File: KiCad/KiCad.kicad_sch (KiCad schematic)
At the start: 24 parts

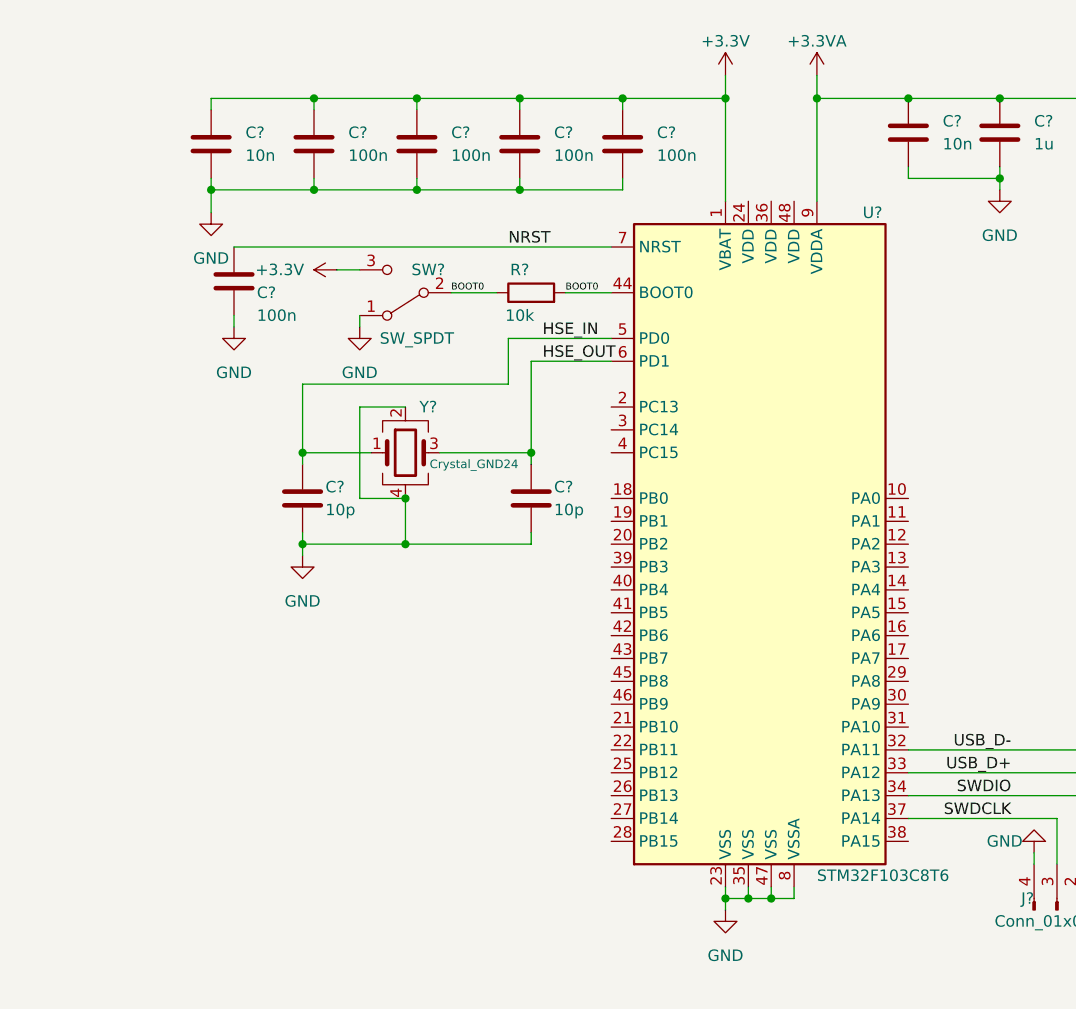
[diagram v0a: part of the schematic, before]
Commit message: Added UART & SPI Support pinout
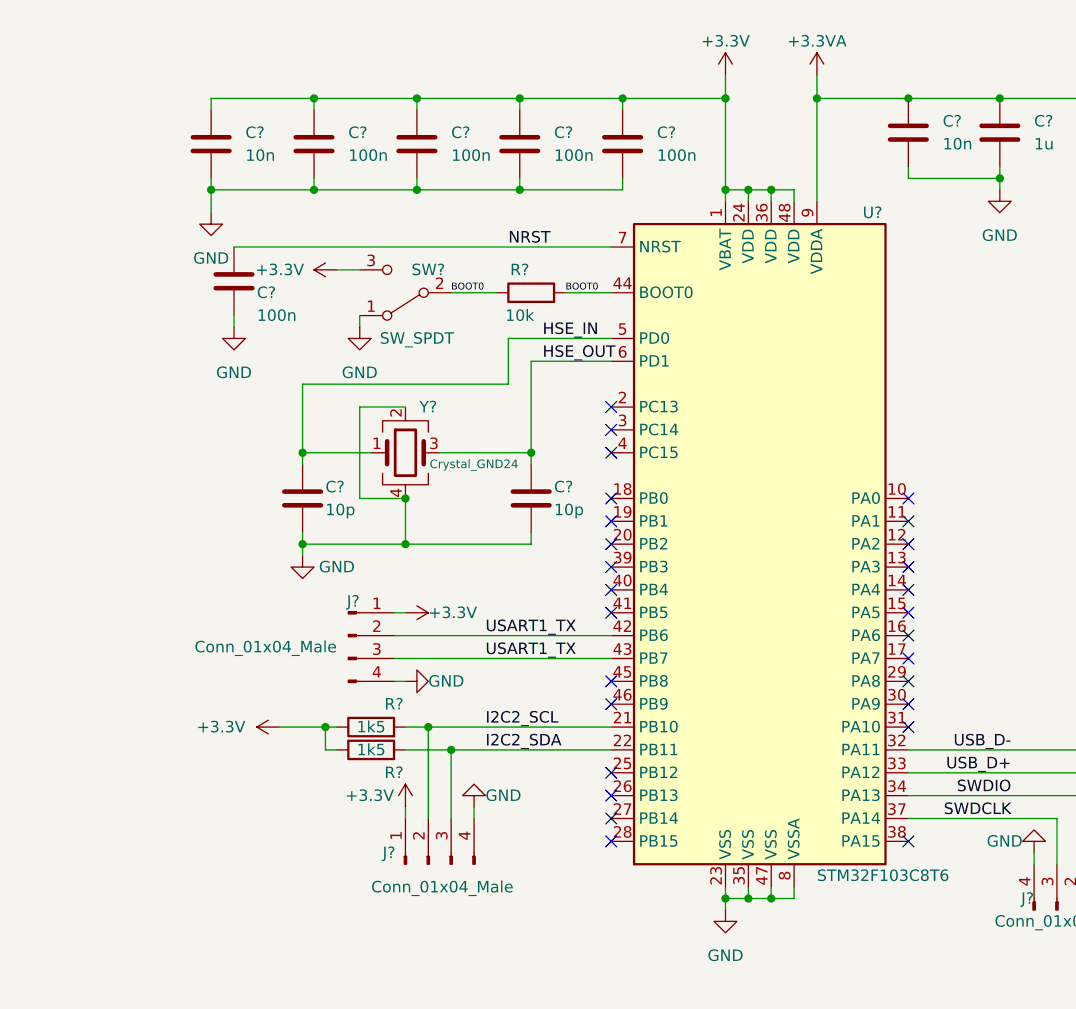
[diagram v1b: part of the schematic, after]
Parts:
- added J? (x2): Conn_01x04_Male, symbol Connector:Conn_01x04_Male
- added R? (x2): 1k5, symbol Device:R
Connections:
- net +3.3V: now also U?.24 (VDD), U?.36 (VDD), U?.48 (VDD), J?.1 (Pin_1), J?.1 (Pin_1), R?.1, R?.1
- net GND: now also J?.4 (Pin_4), J?.4 (Pin_4)
- net I2C2_SCL: now reaches U?.21 (PB10)
- net I2C2_SCL: now also J?.2 (Pin_2), R?.2
- net I2C2_SDA: now reaches U?.22 (PB11)
- net I2C2_SDA: now also J?.3 (Pin_3), R?.2
- net USART1_TX: now reaches U?.42 (PB6)
- net USART1_TX: now also U?.43 (PB7), J?.2 (Pin_2), J?.3 (Pin_3)
- no-connect marks 2 -> 29

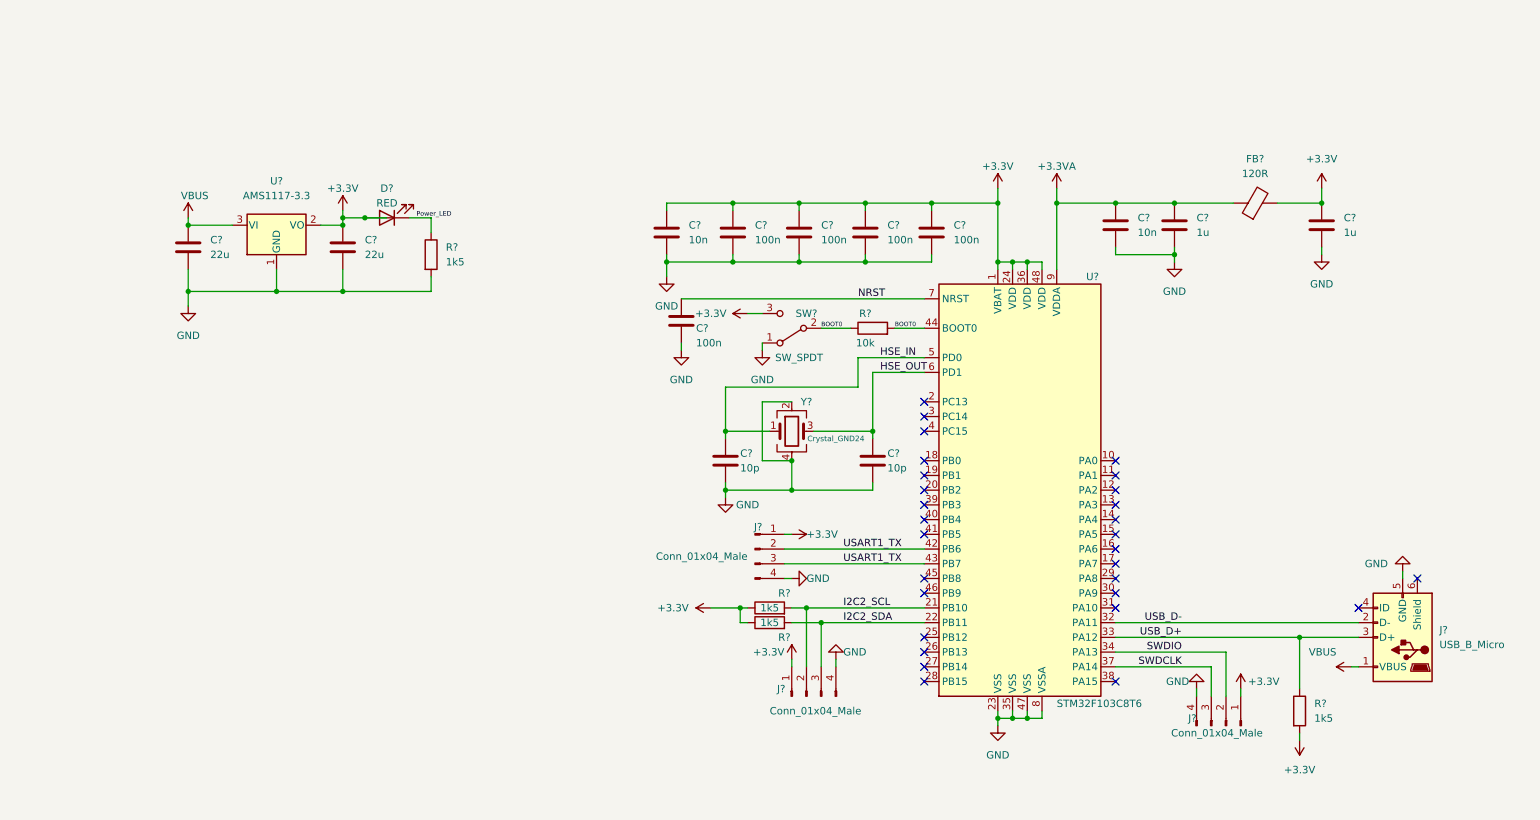
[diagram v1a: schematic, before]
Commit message: Added annotation to schematic
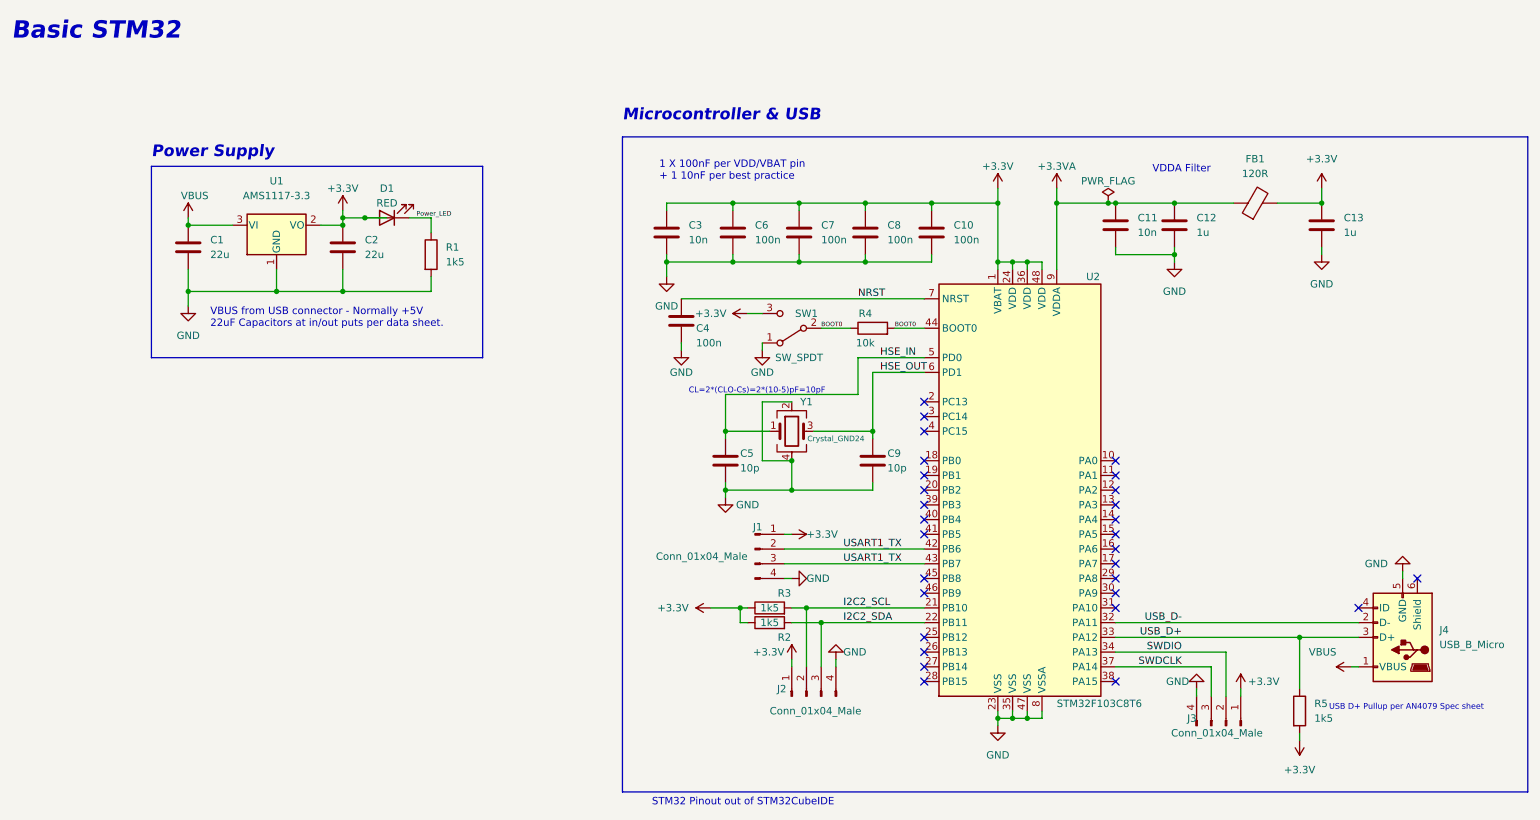
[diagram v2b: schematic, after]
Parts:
- gave numbers to parts that had none: 28
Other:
- note added: "1 X 100nF per VDD/VBAT pin + 1 10nF per best practice"
- note added: "Basic STM32"
- note added: "CL=2*(CLO-Cs)=2*(10-5)pF=10pF"
- note added: "Microcontroller & USB"
- note added: "Power Supply"
- note added: "STM32 Pinout out of STM32CubeIDE"
- note added: "USB D+ Pullup per AN4079 Spec sheet"
- note added: "VBUS from USB connector - Normally +5V 22uF Capacitors at in/out puts per data sheet."
- note added: "VDDA Filter"
- company: (none) -> Sebastian Rincon
- title: (none) -> Basic STM32 Board

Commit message: Added Footprints
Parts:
- C1, C2: footprint (none) -> Capacitor_SMD:C_0805_2012Metric
- C10, C11, C12, C13, C4, C5, C6, C7, C8, C9: footprint (none) -> Capacitor_SMD:C_0402_1005Metric
- C3: value 10n -> 10u; footprint (none) -> Capacitor_SMD:C_0603_1608Metric
- D1: footprint (none) -> LED_SMD:LED_0603_1608Metric
- FB1: footprint (none) -> Inductor_SMD:L_0603_1608Metric
- J1, J2, J3: footprint (none) -> Connector_PinHeader_2.00mm:PinHeader_1x04_P2.00mm_Vertical
- J4: footprint (none) -> Connector_USB:USB_Micro-B_Wuerth_629105150521
- R1, R2, R3, R4, R5: footprint (none) -> Resistor_SMD:R_0402_1005Metric
- SW1: footprint (none) -> Button_Switch_THT:SW_E-Switch_EG1224_SPDT_Angled
- Y1: footprint (none) -> Crystal:Crystal_SMD_3225-4Pin_3.2x2.5mm_HandSoldering
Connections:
- net +3.3V: no longer SW1.3 (C)
- net BOOT0: no longer SW1.2 (B)
- net GND: no longer SW1.1 (A)
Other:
- note added: "1 X 100nF per VDD/VBAT pin + 1 10uF per best practice"
- note removed: "1 X 100nF per VDD/VBAT pin + 1 10nF per best practice"
- moved on the sheet: SW1

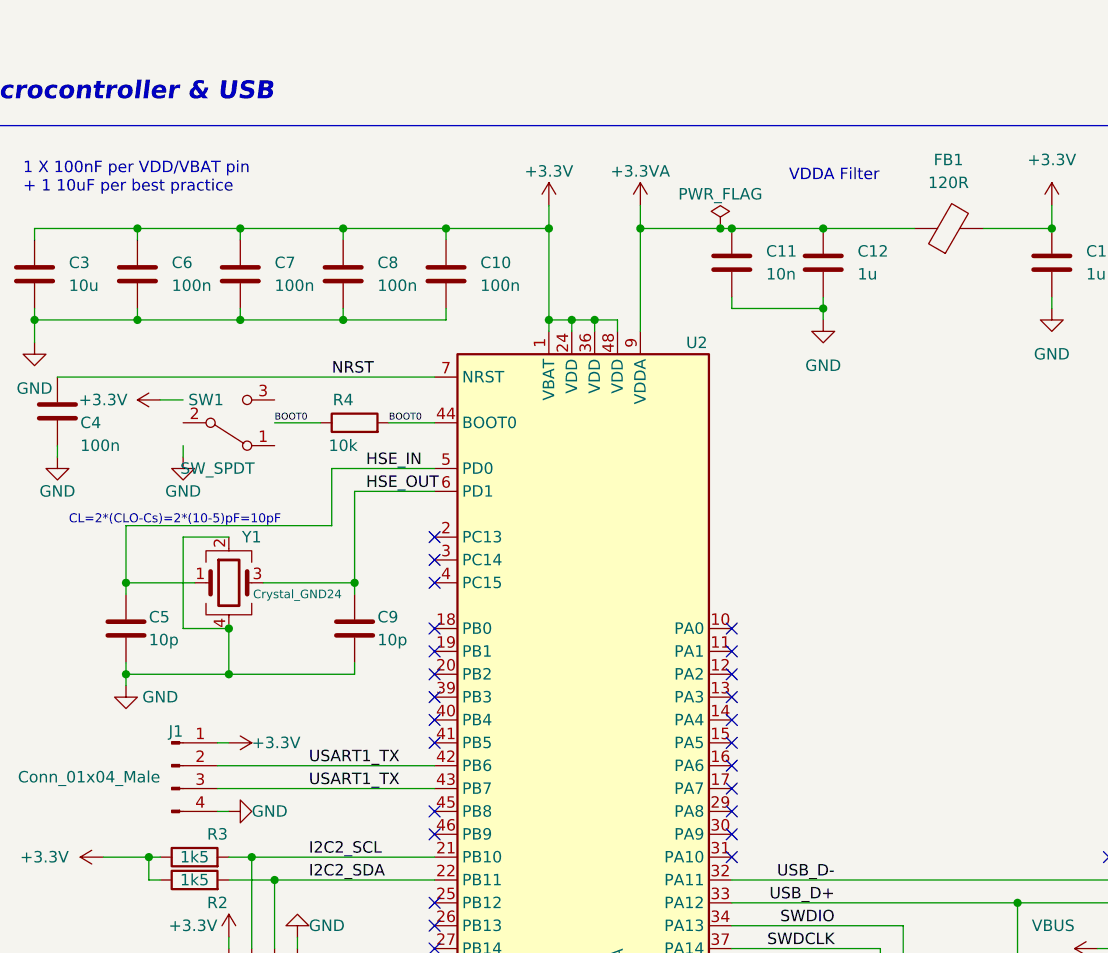
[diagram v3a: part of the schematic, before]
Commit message: Fixed route line bugs & routed pheriphials
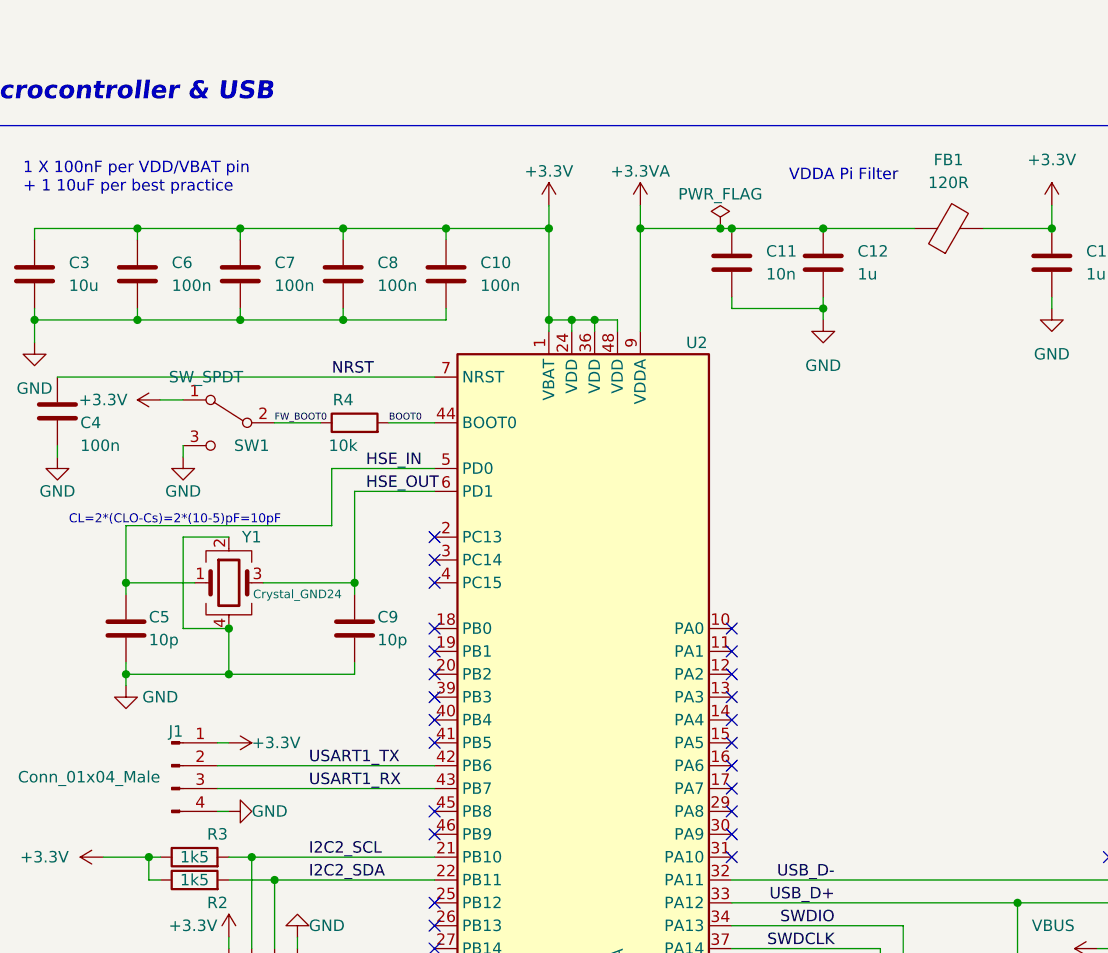
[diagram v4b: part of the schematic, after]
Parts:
- SW1: footprint Button_Switch_THT:SW_E-Switch_EG1224_SPDT_Angled -> Button_Switch_SMD:SW_SPDT_PCM12
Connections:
- net +3.3V: now also SW1.1 (A)
- net BOOT0: no longer R4.1
- net GND: now also SW1.3 (C)
- net USART1_TX: no longer J1.3 (Pin_3), U2.43 (PB7)
- net FW_BOOT0: now reaches SW1.2 (B)
- net FW_BOOT0: now also R4.1
- new net USART1_RX: J1.3 (Pin_3), U2.43 (PB7)
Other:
- note added: "VDDA Pi Filter"
- note removed: "VDDA Filter"
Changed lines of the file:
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@@
   (junction (at 151.13 58.42) (diameter 0) (color 0 0 0 0)
   )
+  (junction (at 128.27 58.42) (diameter 0) (color 0 0 0 0)
+  )
+  (junction (at 162.56 58.42) (diameter 0) (color 0 0 0 0)
+  )
+  (junction (at 139.7 58.42) (diameter 0) (color 0 0 0 0)
+  )
+  (junction (at 185.42 48.26) (diameter 0) (color 0 0 0 0)
+  )
+  (junction (at 187.96 58.42) (diameter 0) (color 0 0 0 0)
+  )
+  (junction (at 215.9 57.15) (diameter 0) (color 0 0 0 0)
+  )
+  (junction (at 162.56 48.26) (diameter 0) (color 0 0 0 0)
+  )
+  (junction (at 72.39 50.8) (diameter 0) (color 0 0 0 0)
+  )
+  (junction (at 45.72 52.07) (diameter 0) (color 0 0 0 0)
+  )
+  (junction (at 215.9 48.26) (diameter 0) (color 0 0 0 0)
+  )
+  (junction (at 152.4 118.11) (diameter 0) (color 0 0 0 0)
+  )
+  (junction (at 204.47 48.26) (diameter 0) (color 0 0 0 0)
+  )
+  (junction (at 241.3 48.26) (diameter 0) (color 0 0 0 0)
+  )
+  (junction (at 195.58 48.26) (diameter 0) (color 0 0 0 0)
+  )
+  (junction (at 140.97 118.11) (diameter 0) (color 0 0 0 0)
+  )
+  (junction (at 138.43 97.79) (diameter 0) (color 0 0 0 0)
+  )
+  (junction (at 237.49 123.19) (diameter 0) (color 0 0 0 0)
+  )
+  (junction (at 72.39 52.07) (diameter 0) (color 0 0 0 0)
+  )
+  (junction (at 173.99 48.26) (diameter 0) (color 0 0 0 0)
+  )
+  (junction (at 187.96 137.16) (diameter 0) (color 0 0 0 0)
+  )
+  (junction (at 60.96 63.5) (diameter 0) (color 0 0 0 0)
+  )
+  (junction (at 138.43 87.63) (diameter 0) (color 0 0 0 0)
+  )
+  (junction (at 72.39 63.5) (diameter 0) (color 0 0 0 0)
+  )
   (junction (at 149.86 92.71) (diameter 0) (color 0 0 0 0)
-  )
-  (junction (at 128.27 58.42) (diameter 0) (color 0 0 0 0)
-  )
-  (junction (at 162.56 58.42) (diameter 0) (color 0 0 0 0)
-  )
-  (junction (at 139.7 58.42) (diameter 0) (color 0 0 0 0)
-  )
-  (junction (at 185.42 48.26) (diameter 0) (color 0 0 0 0)
-  )
-  (junction (at 187.96 58.42) (diameter 0) (color 0 0 0 0)
-  )
-  (junction (at 215.9 57.15) (diameter 0) (color 0 0 0 0)
-  )
-  (junction (at 162.56 48.26) (diameter 0) (color 0 0 0 0)
-  )
-  (junction (at 72.39 50.8) (diameter 0) (color 0 0 0 0)
-  )
-  (junction (at 45.72 52.07) (diameter 0) (color 0 0 0 0)
-  )
-  (junction (at 215.9 48.26) (diameter 0) (color 0 0 0 0)
-  )
-  (junction (at 152.4 118.11) (diameter 0) (color 0 0 0 0)
-  )
-  (junction (at 204.47 48.26) (diameter 0) (color 0 0 0 0)
-  )
-  (junction (at 241.3 48.26) (diameter 0) (color 0 0 0 0)
-  )
-  (junction (at 195.58 48.26) (diameter 0) (color 0 0 0 0)
-  )
-  (junction (at 140.97 118.11) (diameter 0) (color 0 0 0 0)
-  )
-  (junction (at 138.43 97.79) (diameter 0) (color 0 0 0 0)
-  )
-  (junction (at 237.49 123.19) (diameter 0) (color 0 0 0 0)
-  )
-  (junction (at 72.39 52.07) (diameter 0) (color 0 0 0 0)
-  )
-  (junction (at 173.99 48.26) (diameter 0) (color 0 0 0 0)
-  )
-  (junction (at 187.96 137.16) (diameter 0) (color 0 0 0 0)
-  )
-  (junction (at 60.96 63.5) (diameter 0) (color 0 0 0 0)
-  )
-  (junction (at 138.43 87.63) (diameter 0) (color 0 0 0 0)
-  )
-  (junction (at 72.39 63.5) (diameter 0) (color 0 0 0 0)
   )
   (junction (at 185.42 137.16) (diameter 0) (color 0 0 0 0)
@@
     (stroke (width 0) (type default) (color 0 0 0 0))
   )
+  (wire (pts (xy 138.43 87.63) (xy 146.05 87.63))
+    (stroke (width 0) (type default) (color 0 0 0 0))
+  )
   (wire (pts (xy 144.78 72.39) (xy 144.78 73.66))
-    (stroke (width 0) (type default) (color 0 0 0 0))
-  )
-  (wire (pts (xy 138.43 87.63) (xy 146.05 87.63))
     (stroke (width 0) (type default) (color 0 0 0 0))
   )
@@
     (effects (font (size 2 2) bold italic) (justify left bottom))
   )
-  (text "VDDA Filter" (at 212.09 43.18 0)
+  (text "VDDA Pi Filter" (at 212.09 43.18 0)
     (effects (font (size 1.27 1.27)) (justify left bottom))
   )
@@
     (effects (font (size 0.8 0.8)) (justify left bottom))
   )
-  (label "USART1_TX" (at 158.75 110.49 0)
+  (label "USART1_RX" (at 158.75 110.49 0)
     (effects (font (size 1.27 1.27)) (justify left bottom))
   )
@@
     (effects (font (size 0.762 0.762)) (justify left bottom))
   )
-  (label "BOOT0" (at 154.94 69.85 0)
+  (label "FW_BOOT0" (at 154.94 69.85 0)
     (effects (font (size 0.762 0.762)) (justify left bottom))
   )
@@
   )
   (symbol (lib_id "Device:C") (at 139.7 53.34 0) (unit 1)
-    (in_bom yes) (on_board yes) (fields_autoplaced)
-    (property "Reference" "C6" (id 0) (at 143.51 52.0699 0)
+    (in_bom yes) (on_board yes)
+    (property "Reference" "C6" (id 0) (at 143.51 52.07 0)
       (effects (font (size 1.27 1.27)) (justify left))
     )
@@
     (pin "2")
   )
-  (symbol (lib_id "Switch:SW_SPDT") (at 149.86 69.85 0) (mirror x) (unit 1)
-    (in_bom yes) (on_board yes)
-    (property "Reference" "SW1" (id 0) (at 147.32 67.31 0))
-    (property "Value" "SW_SPDT" (id 1) (at 148.59 74.93 0))
-    (property "Footprint" "Button_Switch_THT:SW_E-Switch_EG1224_SPDT_Angled" (id 2) (at 149.86 69.85 0)
+  (symbol (lib_id "Switch:SW_SPDT") (at 149.86 69.85 0) (mirror y) (unit 1)
+    (in_bom yes) (on_board yes)
+    (property "Reference" "SW1" (id 0) (at 152.4 72.39 0))
+    (property "Value" "SW_SPDT" (id 1) (at 147.32 64.77 0))
+    (property "Footprint" "Button_Switch_SMD:SW_SPDT_PCM12" (id 2) (at 149.86 69.85 0)
       (effects (font (size 1.27 1.27)) hide)
     )
@@
     )
     (path "/796ed58e-d24a-4e34-be87-03b344db0b64"
-      (reference "SW1") (unit 1) (value "SW_SPDT") (footprint "Button_Switch_THT:SW_E-Switch_EG1224_SPDT_Angled")
+      (reference "SW1") (unit 1) (value "SW_SPDT") (footprint "Button_Switch_SMD:SW_SPDT_PCM12")
     )
     (path "/7b88c51c-0d15-4478-9932-5f203bb8cfa8"
